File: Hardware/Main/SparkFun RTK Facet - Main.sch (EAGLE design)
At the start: 105 parts, among them J1 QWIIC_RIGHT_ANGLE, J10 FPC_12_0.5MM_BACKFLIP, J15 FPC_12_0.5MM_BACKFLIP, J18 FPC_12_0.5MM_BACKFLIP, J2 U.FL, J8 FPC_12_0.5MM_BACKFLIP, J9 CORTEX_JTAG_DEBUG_PTH, Q2 MBT3904DW1T1, Q3 SIL2308, U1 74HC4052D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

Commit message: Change to NO jumper for I2C pullups
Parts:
- C20: value 22uF -> 10uF; device SparkFun-Capacitors:22UF-0603-6.3V-20% -> SparkFun-Capacitors:10UF-0603-6.3V-20%
- JP7: value JUMPER-SMT_3_2-NC_TRACE_SILK -> JUMPER-SMT_3_NO_SILK; device SparkFun-Jumpers:JUMPER-SMT_3_2-NC_TRACE_SILK -> SparkFun-Jumpers:JUMPER-SMT_3_NO_SILK
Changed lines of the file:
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@@
 <part name="R7" library="SparkFun-Resistors" deviceset="2.2KOHM" device="-0603-1/10W-1%" value="2.2k"/>
 <part name="R12" library="SparkFun-Resistors" deviceset="2.2KOHM" device="-0603-1/10W-1%" value="2.2k"/>
-<part name="JP7" library="SparkFun-Jumpers" deviceset="JUMPER-SMT_3_2-NC_TRACE" device="_SILK" package3d_urn="urn:adsk.eagle:package:39289/1"/>
+<part name="JP7" library="SparkFun-Jumpers" deviceset="JUMPER-SMT_3_NO" device="_SILK" package3d_urn="urn:adsk.eagle:package:39285/1"/>
 <part name="SUPPLY26" library="SparkFun-PowerSymbols" deviceset="3.3V" device=""/>
 <part name="C8" library="SparkFun-Capacitors" deviceset="0.1UF" device="-0603-25V-(+80/-20%)" value="0.1uF"/>
@@
 <part name="J18" library="RTK Facet" deviceset="FPC_12_0.5MM" device="_BACKFLIP" value=""/>
 <part name="Q3" library="SparkFun-DiscreteSemi" deviceset="MOSFET_COMPLIMENTARY_PAIR" device="-SIL2308" value="SIL2308"/>
-<part name="C20" library="SparkFun-Capacitors" deviceset="22UF" device="-0603-6.3V-20%" value="22uF"/>
+<part name="C20" library="SparkFun-Capacitors" deviceset="10UF" device="-0603-6.3V-20%" value="10uF"/>
 <part name="R22" library="SparkFun-Resistors" deviceset="10KOHM" device="-0603-1/10W-1%" value="10k"/>
 <part name="R24" library="SparkFun-Resistors" deviceset="300KOHM" device="-0603-1/10W-1%" value="300k"/>

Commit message: Double up 3.3V rail on Radio connector.
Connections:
- removed net ESP_12/MTDI/RADIO_NI: J10.4, J9.NC/TDI, U5.MISO2/IOA12
- new net ESP_12/MTDI: J9.NC/TDI, U5.MISO2/IOA12
- net 3.3V: now also J10.4
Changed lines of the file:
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@@
 </segment>
 <segment>
-<wire x1="33.02" y1="27.94" x2="33.02" y2="53.34" width="0.1524" layer="91"/>
+<wire x1="33.02" y1="27.94" x2="33.02" y2="30.48" width="0.1524" layer="91"/>
 <pinref part="SUPPLY13" gate="G$1" pin="3.3V"/>
+<wire x1="33.02" y1="30.48" x2="33.02" y2="53.34" width="0.1524" layer="91"/>
 <wire x1="30.48" y1="27.94" x2="33.02" y2="27.94" width="0.1524" layer="91"/>
 <pinref part="J10" gate="J1" pin="3"/>
+<pinref part="J10" gate="J1" pin="4"/>
+<wire x1="30.48" y1="30.48" x2="33.02" y2="30.48" width="0.1524" layer="91"/>
+<junction x="33.02" y="30.48"/>
 </segment>
 </net>
@@
 </segment>
 </net>
-<net name="ESP_12/MTDI/RADIO_NI" class="0">
+<net name="ESP_12/MTDI" class="0">
 <segment>
 <wire x1="215.9" y1="76.2" x2="218.44" y2="76.2" width="0.1524" layer="91"/>
@@
 <label x="393.7" y="91.44" size="1.27" layer="95" xref="yes"/>
 </segment>
-<segment>
-<pinref part="J10" gate="J1" pin="4"/>
-<wire x1="30.48" y1="30.48" x2="35.56" y2="30.48" width="0.1524" layer="91"/>
-<label x="35.56" y="30.48" size="1.27" layer="95" xref="yes"/>
-</segment>
-</net>
+</net>

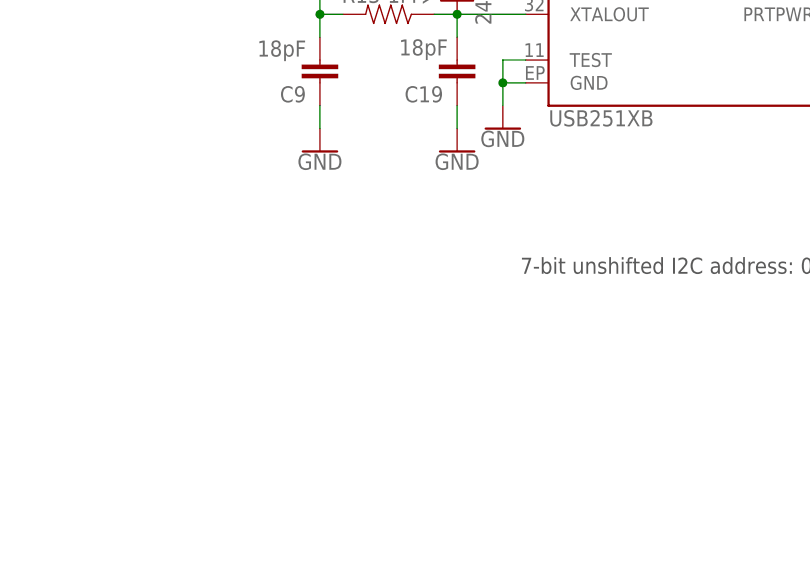
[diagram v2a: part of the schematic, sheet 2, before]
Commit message: Reduce Main, Connector, Display, and Cell board widths by 1mm to allow for v-score protrusion.
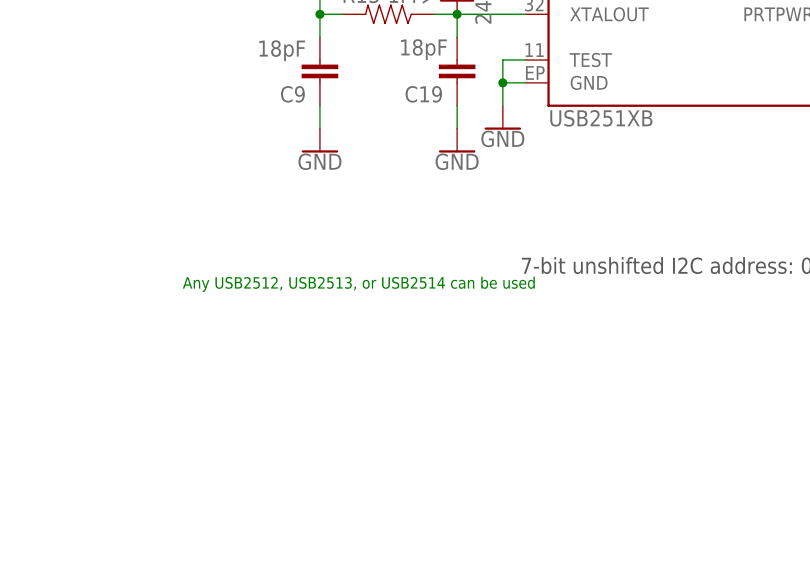
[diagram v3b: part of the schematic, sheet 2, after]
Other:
- note added: "Any USB2512, USB2513, or USB2514 can be used"
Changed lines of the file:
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@@
 <text x="256.54" y="269.24" size="2.54" layer="94" rot="MR180" align="center">USB Hub</text>
 <text x="30.48" y="215.9" size="1.778" layer="97" align="center">Power Button on Membrane Overlay</text>
+<text x="195.58" y="185.42" size="1.27" layer="91">Any USB2512, USB2513, or USB2514 can be used</text>
 </plain>
 <instances>

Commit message: Add revisions to schematics. Add PDFs of schematics.
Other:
- note added: "N. Seidle"
- note added: "v12"
- note removed: "v10"
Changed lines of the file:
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@@
 <sheet>
 <plain>
-<text x="420.624" y="7.366" size="2.54" layer="94">v10</text>
+<text x="420.624" y="7.366" size="2.54" layer="94">v12</text>
 <text x="93.98" y="187.96" size="1.778" layer="97" align="center">7-bit unshifted I2C address: 0x42</text>
 <text x="89.662" y="262.382" size="2.54" layer="94" rot="MR180" align="center">u-blox ZED-F9P</text>
@@
 <text x="279.4" y="78.74" size="1.27" layer="97" align="center">IO5: Has builtin pullup at POR.</text>
 <text x="33.02" y="66.04" size="2.54" layer="94" rot="MR180" align="center">From Radio Board</text>
+<text x="354.33" y="11.43" size="2.54" layer="94">N. Seidle</text>
 </plain>
 <instances>

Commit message: Move thermistor from heat sources.
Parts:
- U5: value ESP-WROOM-3232D-NARROW -> ESP-WROOM-3232D; device SparkFun-RF:ESP-WROOM-3232D-NARROW -> SparkFun-RF:ESP-WROOM-3232D
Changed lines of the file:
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@@
 <grid distance="0.1" unitdist="inch" unit="inch" style="lines" multiple="1" display="no" altdistance="0.01" altunitdist="inch" altunit="inch"/>
 <layers>
-<layer number="1" name="Top" color="4" fill="1" visible="no" active="no"/>
-<layer number="2" name="Route2" color="1" fill="3" visible="no" active="no"/>
-<layer number="3" name="Route3" color="4" fill="3" visible="no" active="no"/>
-<layer number="4" name="Route4" color="1" fill="4" visible="no" active="no"/>
-<layer number="5" name="Route5" color="4" fill="4" visible="no" active="no"/>
-<layer number="6" name="Route6" color="1" fill="8" visible="no" active="no"/>
-<layer number="7" name="Route7" color="4" fill="8" visible="no" active="no"/>
-<layer number="8" name="Route8" color="1" fill="2" visible="no" active="no"/>
-<layer number="9" name="Route9" color="4" fill="2" visible="no" active="no"/>
-<layer number="10" name="Route10" color="1" fill="7" visible="no" active="no"/>
-<layer number="11" name="Route11" color="4" fill="7" visible="no" active="no"/>
-<layer number="12" name="Route12" color="1" fill="5" visible="no" active="no"/>
-<layer number="13" name="Route13" color="4" fill="5" visible="no" active="no"/>
-<layer number="14" name="Route14" color="1" fill="6" visible="no" active="no"/>
-<layer number="15" name="Route15" color="4" fill="6" visible="no" active="no"/>
-<layer number="16" name="Bottom" color="1" fill="1" visible="no" active="no"/>
-<layer number="17" name="Pads" color="2" fill="1" visible="no" active="no"/>
-<layer number="18" name="Vias" color="2" fill="1" visible="no" active="no"/>
-<layer number="19" name="Unrouted" color="6" fill="1" visible="no" active="no"/>
-<layer number="20" name="Dimension" color="24" fill="1" visible="no" active="no"/>
-<layer number="21" name="tPlace" color="16" fill="1" visible="no" active="no"/>
-<layer number="22" name="bPlace" color="14" fill="1" visible="no" active="no"/>
-<layer number="23" name="tOrigins" color="15" fill="1" visible="no" active="no"/>
-<layer number="24" name="bOrigins" color="15" fill="1" visible="no" active="no"/>
-<layer number="25" name="tNames" color="7" fill="1" visible="no" active="no"/>
-<layer number="26" name="bNames" color="7" fill="1" visible="no" active="no"/>
-<layer number="27" name="tValues" color="7" fill="1" visible="no" active="no"/>
-<layer number="28" name="bValues" color="7" fill="1" visible="no" active="no"/>
+<layer number="1" name="Top" color="4" fill="1" visible="yes" active="no"/>
+<layer number="2" name="Route2" color="1" fill="3" visible="yes" active="no"/>
+<layer number="3" name="Route3" color="4" fill="3" visible="yes" active="no"/>
+<layer number="4" name="Route4" color="1" fill="4" visible="yes" active="no"/>
+<layer number="5" name="Route5" color="4" fill="4" visible="yes" active="no"/>
+<layer number="6" name="Route6" color="1" fill="8" visible="yes" active="no"/>
+<layer number="7" name="Route7" color="4" fill="8" visible="yes" active="no"/>
+<layer number="8" name="Route8" color="1" fill="2" visible="yes" active="no"/>
+<layer number="9" name="Route9" color="4" fill="2" visible="yes" active="no"/>
+<layer number="10" name="Route10" color="1" fill="7" visible="yes" active="no"/>
+<layer number="11" name="Route11" color="4" fill="7" visible="yes" active="no"/>
+<layer number="12" name="Route12" color="1" fill="5" visible="yes" active="no"/>
+<layer number="13" name="Route13" color="4" fill="5" visible="yes" active="no"/>
+<layer number="14" name="Route14" color="1" fill="6" visible="yes" active="no"/>
+<layer number="15" name="Route15" color="4" fill="6" visible="yes" active="no"/>
+<layer number="16" name="Bottom" color="1" fill="1" visible="yes" active="no"/>
+<layer number="17" name="Pads" color="2" fill="1" visible="yes" active="no"/>
+<layer number="18" name="Vias" color="2" fill="1" visible="yes" active="no"/>
+<layer number="19" name="Unrouted" color="6" fill="1" visible="yes" active="no"/>
+<layer number="20" name="Dimension" color="24" fill="1" visible="yes" active="no"/>
+<layer number="21" name="tPlace" color="16" fill="1" visible="yes" active="no"/>
+<layer number="22" name="bPlace" color="14" fill="1" visible="yes" active="no"/>
+<layer number="23" name="tOrigins" color="15" fill="1" visible="yes" active="no"/>
+<layer number="24" name="bOrigins" color="15" fill="1" visible="yes" active="no"/>
+<layer number="25" name="tNames" color="7" fill="1" visible="yes" active="no"/>
+<layer number="26" name="bNames" color="7" fill="1" visible="yes" active="no"/>
+<layer number="27" name="tValues" color="7" fill="1" visible="yes" active="no"/>
+<layer number="28" name="bValues" color="7" fill="1" visible="yes" active="no"/>
 <layer number="29" name="tStop" color="7" fill="3" visible="no" active="no"/>
 <layer number="30" name="bStop" color="7" fill="6" visible="no" active="no"/>
@@
 <layer number="35" name="tGlue" color="7" fill="4" visible="no" active="no"/>
 <layer number="36" name="bGlue" color="7" fill="5" visible="no" active="no"/>
-<layer number="37" name="tTest" color="7" fill="1" visible="no" active="no"/>
-<layer number="38" name="bTest" color="7" fill="1" visible="no" active="no"/>
+<layer number="37" name="tTest" color="7" fill="1" visible="yes" active="no"/>
+<layer number="38" name="bTest" color="7" fill="1" visible="yes" active="no"/>
 <layer number="39" name="tKeepout" color="4" fill="11" visible="no" active="no"/>
 <layer number="40" name="bKeepout" color="1" fill="11" visible="no" active="no"/>
@@
 <layer number="44" name="Drills" color="7" fill="1" visible="no" active="no"/>
 <layer number="45" name="Holes" color="7" fill="1" visible="no" active="no"/>
-<layer number="46" name="Milling" color="3" fill="1" visible="no" active="no"/>
-<layer number="47" name="Measures" color="7" fill="1" visible="no" active="no"/>
-<layer number="48" name="Document" color="7" fill="1" visible="no" active="no"/>
-<layer number="49" name="Reference" color="7" fill="1" visible="no" active="no"/>
-<layer number="50" name="dxf" color="7" fill="1" visible="no" active="no"/>
-<layer number="51" name="tDocu" color="6" fill="1" visible="no" active="no"/>
-<layer number="52" name="bDocu" color="7" fill="1" visible="no" active="no"/>
-<layer number="53" name="tGND_GNDA" color="7" fill="9" visible="no" active="no"/>
-<layer number="54" name="bGND_GNDA" color="1" fill="9" visible="no" active="no"/>
-<layer number="56" name="wert" color="7" fill="1" visible="no" active="no"/>
-<layer number="57" name="tCAD" color="7" fill="1" visible="no" active="no"/>
-<layer number="59" name="tCarbon" color="7" fill="1" visible="no" active="no"/>
-<layer number="60" name="bCarbon" color="7" fill="1" visible="no" active="no"/>
+<layer number="46" name="Milling" color="3" fill="1" visible="yes" active="no"/>
+<layer number="47" name="Measures" color="7" fill="1" visible="yes" active="no"/>
+<layer number="48" name="Document" color="7" fill="1" visible="yes" active="no"/>
+<layer number="49" name="Reference" color="7" fill="1" visible="yes" active="no"/>
+<layer number="50" name="dxf" color="7" fill="1" visible="yes" active="no"/>
+<layer number="51" name="tDocu" color="6" fill="1" visible="yes" active="no"/>
+<layer number="52" name="bDocu" color="7" fill="1" visible="yes" active="no"/>
+<layer number="53" name="tGND_GNDA" color="7" fill="9" visible="yes" active="no"/>
+<layer number="54" name="bGND_GNDA" color="1" fill="9" visible="yes" active="no"/>
+<layer number="56" name="wert" color="7" fill="1" visible="yes" active="no"/>
+<layer number="57" name="tCAD" color="7" fill="1" visible="yes" active="no"/>
+<layer number="59" name="tCarbon" color="7" fill="1" visible="yes" active="no"/>
+<layer number="60" name="bCarbon" color="7" fill="1" visible="yes" active="no"/>
 <layer number="88" name="SimResults" color="9" fill="1" visible="yes" active="yes"/>
 <layer number="89" name="SimProbes" color="9" fill="1" visible="yes" active="yes"/>
@@
 <part name="GND9" library="SparkFun-PowerSymbols" deviceset="GND" device=""/>
 <part name="J8" library="RTK Facet" deviceset="FPC_12_0.5MM" device="_BACKFLIP" value=""/>
-<part name="U5" library="SparkFun-RF" deviceset="ESP-WROOM-32" device="32D-NARROW"/>
+<part name="U5" library="SparkFun-RF" deviceset="ESP-WROOM-32" device="32D" value="ESP-WROOM-3232D"/>
 <part name="JP1" library="SparkFun-Jumpers" deviceset="JUMPER-SMT_2_NO" device="_SILK" package3d_urn="urn:adsk.eagle:package:39279/1" value=""/>
 <part name="JP2" library="SparkFun-Jumpers" deviceset="JUMPER-SMT_2_NO" device="_SILK" package3d_urn="urn:adsk.eagle:package:39279/1" value=""/>

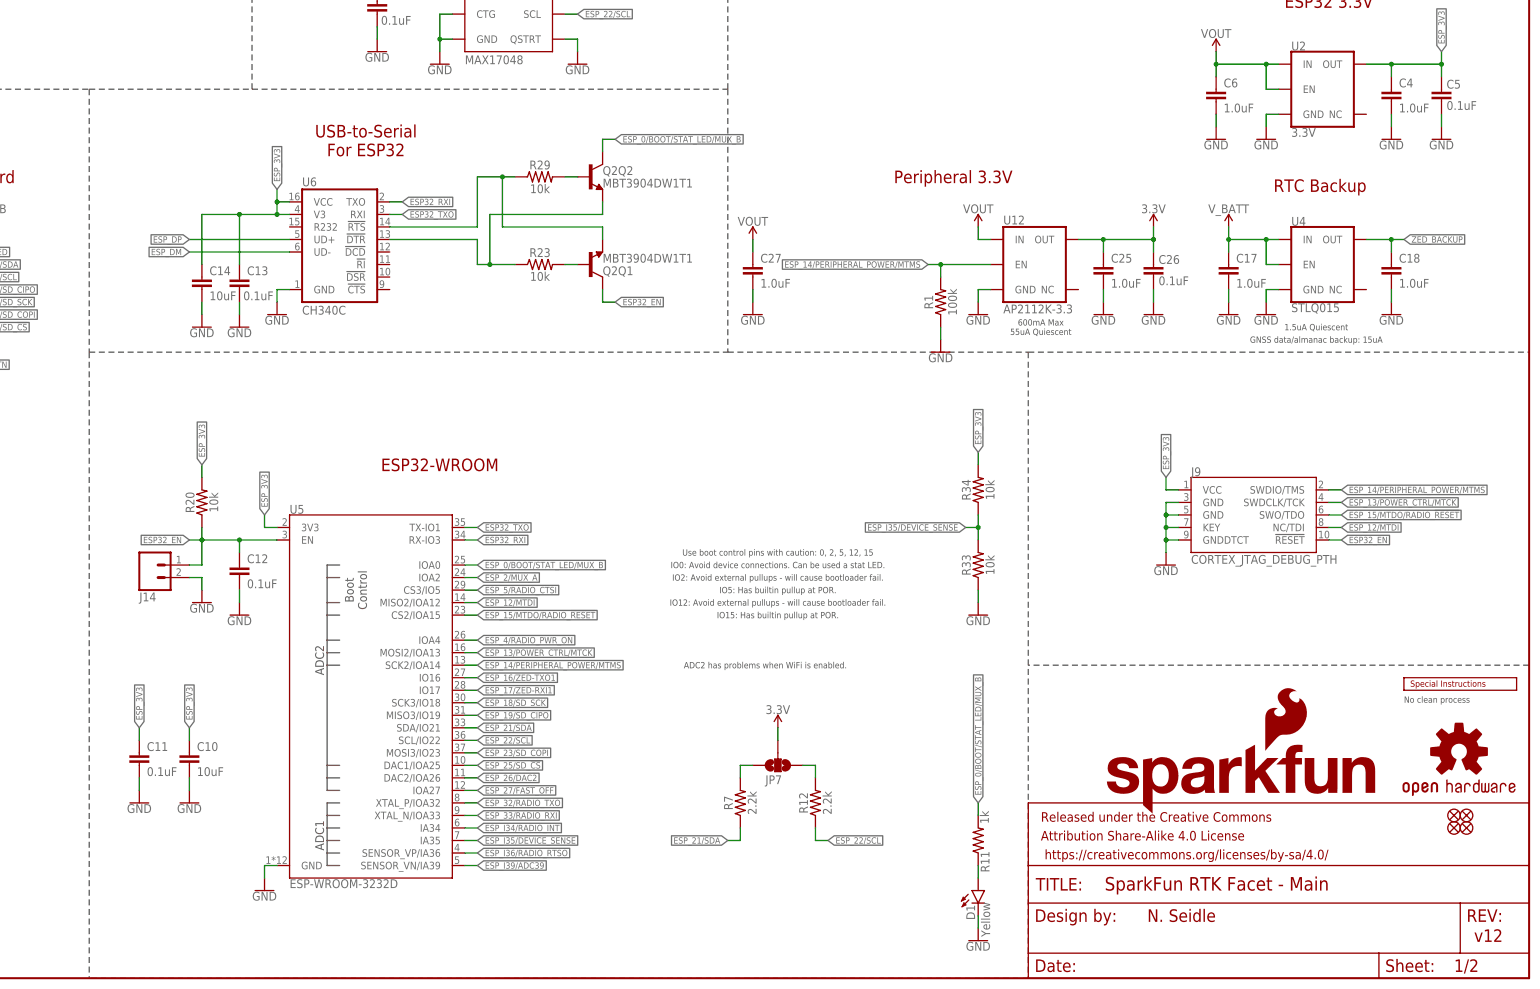
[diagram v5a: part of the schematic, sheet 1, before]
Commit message: Add IDs to schematic
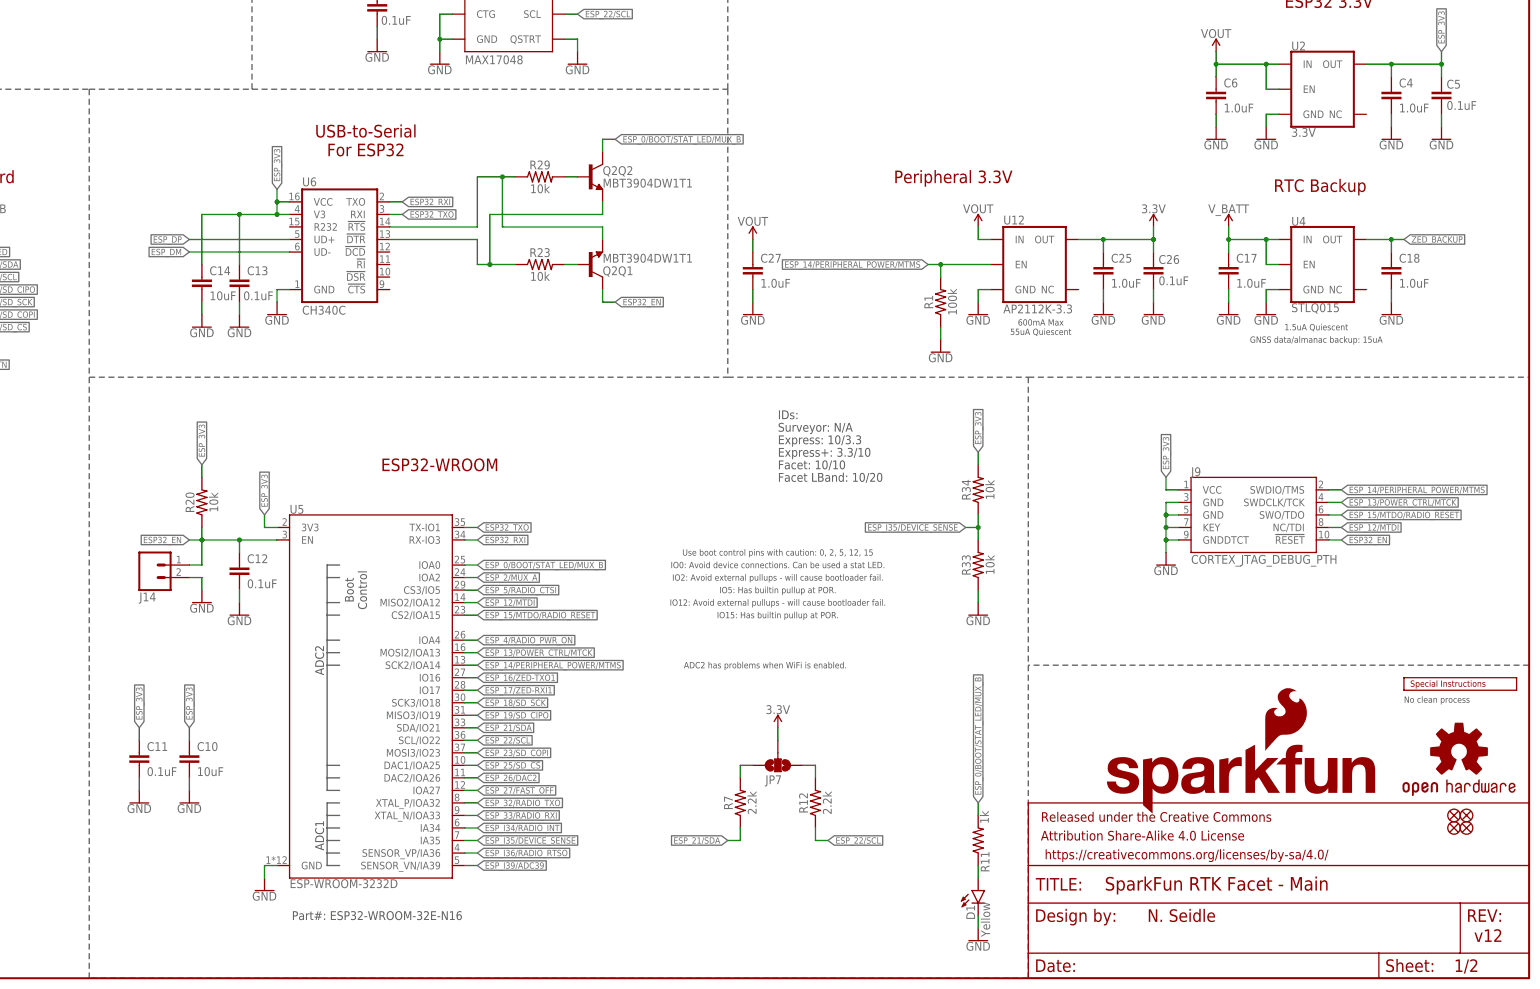
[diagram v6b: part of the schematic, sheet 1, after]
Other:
- note added: "Express+: 3.3/10"
- note added: "Express: 10/3.3"
- note added: "Facet LBand: 10/20"
- note added: "Facet: 10/10"
- note added: "IDs:"
- note added: "Part#: ESP32-WROOM-32E-N16"
- note added: "Surveyor: N/A"
